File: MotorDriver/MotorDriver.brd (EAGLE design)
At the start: 50 x 50 mm, 58 parts, among them CN1 53375-0610, Q1 BUK7Y7R8-80EX, Q2 BUK7Y7R8-80EX, Q3 BUK7Y7R8-80EX, Q4 BUK7Y7R8-80EX, Q5 BUK7Y7R8-80EX, Q6 BUK7Y7R8-80EX, U1 LPC1549JBD48, U2 DRV8320SRTVT, U3 MCP1700T-33, U4 ADR5041

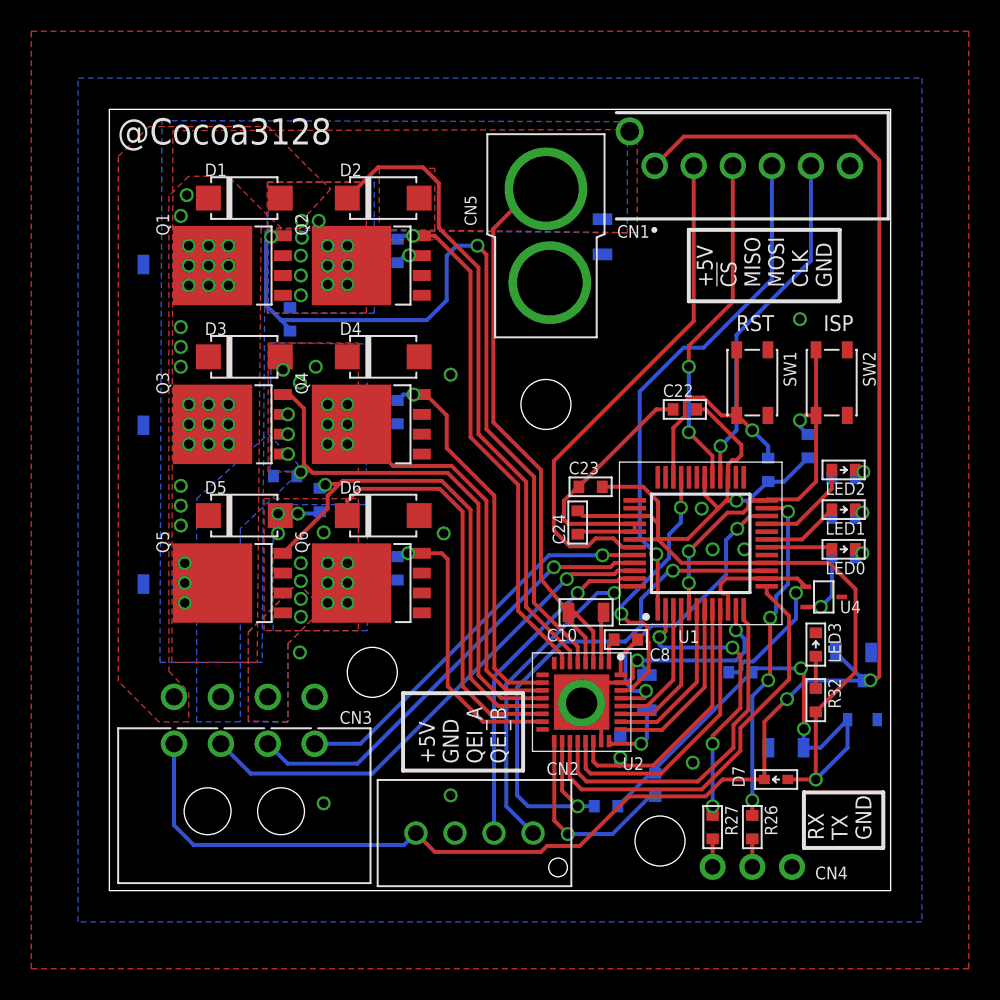
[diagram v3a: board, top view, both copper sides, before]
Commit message: 機能追加 *CANバス *ホールセンサをダイレクトでDRVへ入力 *電源電圧監視 *DCDCをGDに内蔵 *15Aヒューズ
機能削減
*UART-DFUを廃止
*SPI接続を廃止
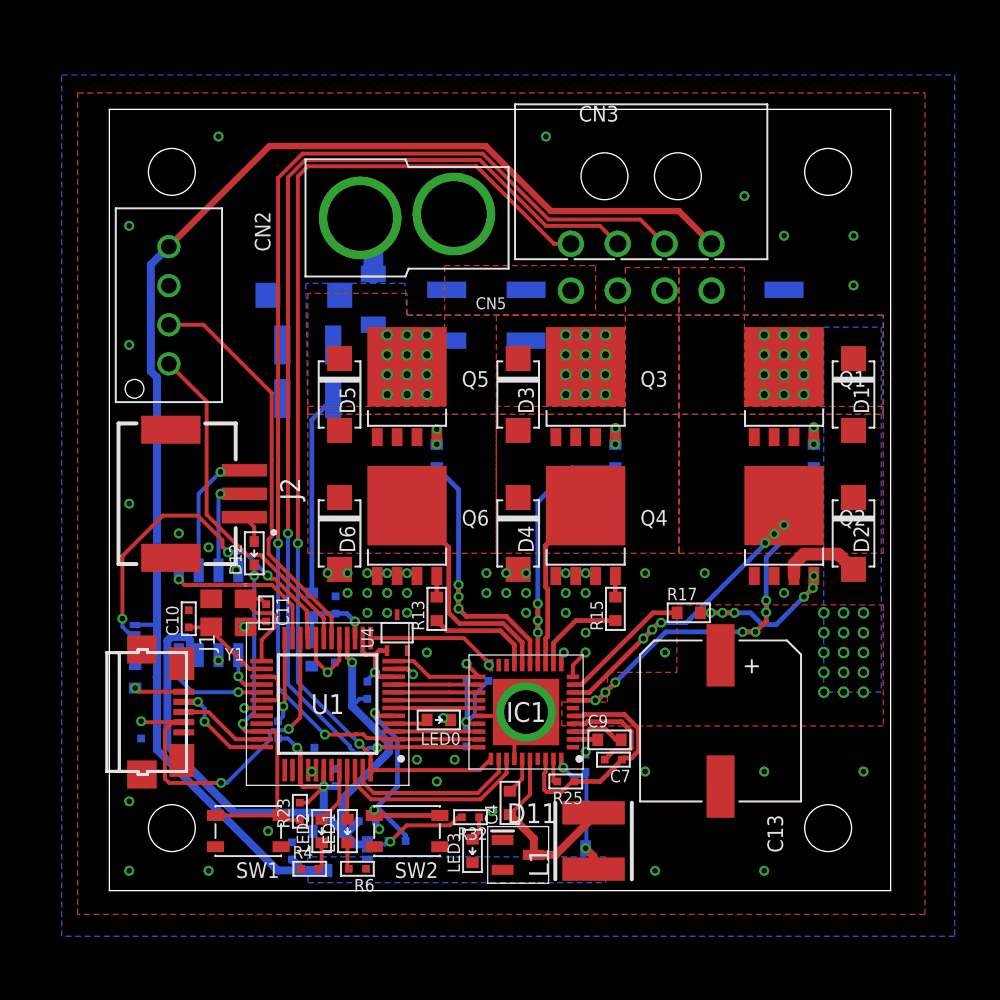
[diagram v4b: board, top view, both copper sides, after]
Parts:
- removed CN1: 53375-0610, MotorDriver:53375-0610
- removed CN4: (no value), nonolith.lbr:1X03_ROUND
- removed R10, R11, R12, R9: 10k, MotorDriver:R1608
- removed R26, R27: 100, MotorDriver:R1608
- removed U2: DRV8320SRTVT, MotorDriver:DRV8320SRTVT
- added C11: 10p, MotorDriver:C1005
- added C12: 10u, MotorDriver:C3225
- added C13: 100u, Passive:ES-10
- added C4: 0.1u, MotorDriver:C1608
- added C5: 0.47u, MotorDriver:C1005
- added C7: 1u, MotorDriver:C1005
- added D10: SMAJ60A, MotorDriver:DO-214AC
- added D11: HSMS-2800-TR1G, HSMS-2800-TR1G:SOT96P240X120-3N
- added D12: (no value), MotorDriver:DIODE_SOD523
- added D8, D9: SDM2U40CSP-7B, SDM2U40CSP-7B:X3-WLB1608-2
- added F1: 15, Passive:3216
- added IC1: DRV8320RSRHAR, DRV8320RSRHAR:QFN50P600X600X100-41N
- added IC2: MAX3051ESA+, MAX3051ESA+:SOIC127P600X175-8N
- added J1: J_USB_MICROAB_HIROSE_ZX62-AB-5PA, j_usb_hirose_zx62-ab-5pa:J_USB_MICROAB_HIROSE_ZX62-AB-5PA
- added J2: SM03B-ZESS-TB, SM03B-ZESS-TB:SM03B-ZESS-TB
- added L1: NR5040T330M, NR5040T330M:NR5040T2R2N
- added R13, R14, R15, R16: 10, MotorDriver:R1608
- added R18: (no value), MotorDriver:R1005
- added R19, R24: 10k, MotorDriver:R1005
- added R20: 47k, MotorDriver:R1608
- added R22: 2.2k, MotorDriver:R1608
- added R25: 100k, MotorDriver:R1005
- added RF1: 900m, Passive:1608
- added Y1: FA238V, FA238V:EPSON_FA238V
- C1, C2, C3, C6: value 1u -> 10u; device MotorDriver:C2012 -> MotorDriver:C3225
- C10: value 1u -> 10p; device MotorDriver:C2012 -> MotorDriver:C1005
- C19, C20: value 1u -> 0.1u; device MotorDriver:C2012 -> MotorDriver:C1005
- C22, C23, C24: device MotorDriver:C1608 -> MotorDriver:C1005
- C8: value 47n -> 1u; device MotorDriver:C1608 -> MotorDriver:C1005
- C9: value 1u -> 47n; device MotorDriver:C2012 -> MotorDriver:C1608
- D1, D2, D3, D4, D5, D6: value (none) -> NRVTSA4100ET3G
- D7: value (none) -> SDM2U40CSP-7B; device MotorDriver:DIODE_SOD523 -> SDM2U40CSP-7B:X3-WLB1608-2
- R1: value 10k -> 12k; device MotorDriver:R1608 -> MotorDriver:R1005
- R17, R3: value 10k -> 10
- R2: value 10k -> 2.2k; device MotorDriver:R1608 -> MotorDriver:R1005
- R21, R23, R32, R4, R5, R6, R7, R8: device MotorDriver:R1608 -> MotorDriver:R1005
- SW1, SW2: device Switch:SKRP -> MotorDriver:SKRP
- U3: device ic-Microchip:SOT23-3 -> MotorDriver:SOT23-3
- U4: device ic-AD:SC70-3 -> MotorDriver:SC70-3
- moved CN3 47.9 mm to (34.0, 45.7), turned to 0 degrees
- moved SW1 43.2 mm to (8.89, 3.81), turned to 180 degrees
- moved R4 42.3 mm to (12.8, 1.40), flipped to the top, turned to 0 degrees
- moved D1 41.0 mm to (47.6, 31.8), turned to 270 degrees
- moved LED2 40.6 mm to (13.6, 3.81), turned to 90 degrees
- moved C1 40.0 mm to (43.2, 36.8), turned to 90 degrees
- moved SW2 39.5 mm to (19.1, 3.81), turned to 180 degrees
- moved CN2 39.0 mm to (3.81, 37.5), turned to 270 degrees
- moved R6 38.4 mm to (15.9, 1.40), flipped to the top
- moved C20 38.1 mm to (11.7, 2.54), turned to 90 degrees
- moved LED1 37.8 mm to (15.2, 3.81), turned to 90 degrees
- moved R23 37.1 mm to (12.2, 5.08), flipped to the top, turned to 90 degrees
- moved D2 37.0 mm to (47.6, 22.9), turned to 270 degrees
- moved Q1 35.8 mm to (43.2, 31.8), turned to 0 degrees
- moved U3 35.6 mm to (14.0, 2.54), turned to 180 degrees
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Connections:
- removed net !CS_DEV: CN1.2, U1.43
- removed net MISO: CN1.3, U1.29
- removed net MOSI: CN1.4, U1.1
- removed net PWM_AL: U1.6, U2.26
- removed net PWM_BH: U1.4, U2.27
- removed net PWM_BL: U1.3, U2.28
- removed net PWM_CH: U1.22, U2.29
- removed net PWM_CL: U1.33, U2.30
- removed net RX: R27.1, U1.2
- removed net SCLK_DEV: CN1.5, U1.28
- removed net TX: R26.1, U1.23
- new net !BRAKE: IC1.33, U1.46
- new net CANH: IC2.7, J2.2
- new net CANL: IC2.6, J2.3
- new net CAN_RX: IC2.4, U1.29
- new net CAN_TX: IC2.1, U1.28
- new net D+: J1.P$3, U1.35
- new net D-: J1.P$2, U1.36
- new net DIR: IC1.32, U1.47
- new net ID: J1.P$4, R8.2, U1.22
- new net N$11: Q3.4, R14.2
- new net N$12: Q6.4, R13.2
- new net N$13: Q5.4, R3.2
- new net N$14: J1.P$1, RF1.1
- new net N$15: R18.2, U1.24
- new net N$16: C7.2, IC1.4
- new net N$17: C8.1, IC1.27, R19.2, R24.2
- new net N$18: C9.1, IC1.2
- new net N$19: C9.2, IC1.3
- new net N$20: IC1.39, R25.2
- new net N$21: C11.1, U1.25, Y1.1
- new net N$22: C10.1, U1.26, Y1.3
- new net N$23: U1.27, U1.30
- new net N$24: D12.A, J2.1
- new net N$26: CN5.P, F1.2
- new net N$4: C4.2, IC1.35
- new net SHDN: IC2.5, U1.23
- new net VBAT: C5.2, R20.1, R22.2, U1.15
- new net VBUS: D9.2, RF1.2, U1.21
- net !CS: now also IC1.24, U1.7; no longer U1.9, U2.21
- net !FAULT: now also IC1.20, R24.1, U1.13; no longer R1.1, U2.17
- net !ISP: now also R7.1; no longer R17.1, U1.24
- net !RST: now also D12.K
- net +3V3: now also D7.2, IC2.3, R18.1, R7.2; no longer D7.A, R1.2, R17.2, R2.2, U1.27, U1.30
- net +5V: now also D7.1, D8.1, D9.1; no longer CN1.1, D7.K
- net GH_A: now also IC1.7, R16.1; no longer Q1.4, R11.2, U2.5
- net GH_B: now also IC1.14, R14.1; no longer Q3.4, R9.2, U2.12
- net GH_C: now also IC1.15, R3.1; no longer Q5.4, R7.2, U2.13
- net GL_A: now also IC1.9, R17.1; no longer Q2.4, R12.2, U2.7
- net GL_B: now also IC1.12, R15.1; no longer Q4.4, R10.2, U2.10
- net GL_C: now also IC1.17, R13.1; no longer Q6.4, R8.2, U2.15
- net GND: now also C10.2, C11.2, C12.2, C13.N, C5.1, C8.2, CN3.6, D10.A, D11.1, IC1.1, IC1.10, IC1.11, IC1.18, IC1.19, IC1.26, IC1.34, IC1.41, IC2.2, IC2.8, J1.P$5, J1.SHIELD1, J1.SHIELD2, J1.SHIELD3, J1.SHIELD4, R2.2, R22.1, Y1.2, Y1.4; no longer C9.2, CN1.6, CN3.5, CN4.1, R10.1, R12.1, R3.1, U2.16, U2.23, U2.31, U2.33, U2.8, U2.9
- net HALL_U: now also IC1.29, U1.2; no longer U1.46
- net HALL_V: now also IC1.30, U1.1; no longer U1.45
- net HALL_W: now also IC1.31, U1.48; no longer U1.44
- net LED0: now also U1.4; no longer U1.18
- net LED1: now also U1.45; no longer U1.19
- net LED2: now also U1.44; no longer U1.21
- net N$1: now also IC1.40, R1.2, R2.1; no longer CN4.2, R26.2
- net N$2: now also D8.2, L1.1, R1.1; no longer CN4.3, R27.2
- net N$3: now also C4.1, D11.3, IC1.36, L1.2; no longer C10.1, U2.2
- net N$5: now also Q2.4, R17.2; no longer C8.1, U2.1
- net N$6: now also Q1.4, R16.2; no longer C8.2, U2.32
- net N$7: now also Q4.4, R15.2; no longer C9.1, U2.24
- net PWM_AH: now also IC1.28, U1.3; no longer U1.7, U2.25
- net PWM_EN: now also IC1.25, U1.6; no longer R3.2, U1.8, U2.22
- net QEI_A: now also U1.18; no longer U1.47
- net QEI_B: now also U1.19; no longer U1.48
- net SCLK: now also IC1.23, U1.8; no longer U1.12, U2.20
- net SDI: now also IC1.22, U1.9; no longer U1.13, U2.19
- net SDO: now also IC1.21, R19.1, U1.12; no longer R2.1, U1.15, U2.18
- net SH_A: now also IC1.8; no longer R11.1, U2.6
- net SH_B: now also IC1.13; no longer R9.1, U2.11
- net SH_C: now also CN3.5, IC1.16; no longer CN3.6, R7.1, U2.14
- net V+: now also C12.1, C13.P, C7.1, D10.K, F1.1, IC1.38, IC1.5, IC1.6, R20.2, R25.1; no longer C10.2, CN5.P, U2.3, U2.4
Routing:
- net HALL_W: track 25.5 -> 67.7 mm, vias 1 -> 2
- net HALL_U: track 32.7 -> 74.7 mm, vias 1 -> 2
- net HALL_V: track 29.3 -> 70.5 mm, vias 1 -> 2
- net +3V3: track 93.6 -> 60.0 mm
- net MOSI: track 33.1 -> 0.00 mm, vias 1 -> 0
- net !CS_DEV: track 33.1 -> 0.00 mm
- net SDO: track 36.8 -> 7.07 mm, vias 2 -> 1
- net VBUS: track 0.00 -> 24.7 mm, vias 0 -> 3
- net GL_A: track 33.2 -> 8.57 mm, vias 1 -> 0
- net GH_A: track 53.2 -> 28.9 mm, vias 2 -> 7
- net ID: track 0.00 -> 23.1 mm, vias 0 -> 3
- net SCLK_DEV: track 22.3 -> 0.00 mm, vias 1 -> 0
- net GND: track 45.6 -> 23.4 mm, vias 15 -> 66
- net TX: track 21.9 -> 0.00 mm, vias 4 -> 0
- net MISO: track 21.7 -> 0.00 mm, vias 2 -> 0
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- added copper zone on layer 16, net +5V
- removed copper zone on layer 16, net SH_A
- removed copper zone on layer 16, net SH_B
- removed copper zone on layer 16, net SH_C
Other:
- board text removed: "+5V !CS MISO MOSI CLK GND"
- board text removed: "+5V GND QEI_A QEI_B"
- board text removed: "@Cocoa3128"
- board text removed: "ISP"
- board text removed: "RST"
- board text removed: "RX TX GND"

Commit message: ヒューズ切断検出機能を追加
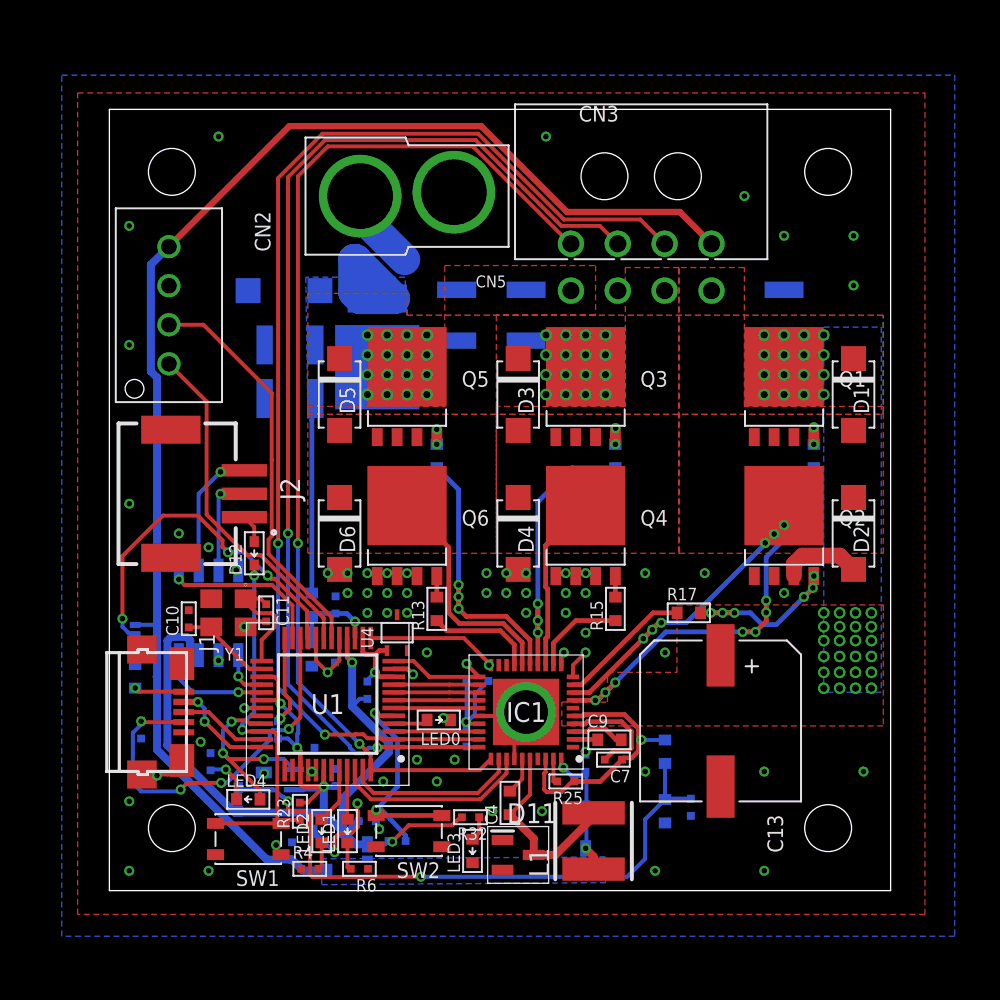
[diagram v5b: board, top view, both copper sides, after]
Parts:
- added C14: 0.47u, MotorDriver:C1005
- added D13: TSPB20U80S S1G, Diode:SMPC
- added D14: RB520S, MotorDriver:DIODE_SOD523
- added LED4: (no value), MotorDriver:LED1608
- added R10: 2.2k, MotorDriver:R1608
- added R11: 330, MotorDriver:R1005
- added R9: 33k, MotorDriver:R1608
- added U2: ADCMP350YKSZ, adcmp350:KS_4
- moved F1 2.57 mm to (17.3, 40.4), turned to 180 degrees
- moved CN5 1.40 mm to (19.1, 44.5)
- moved D10 1.30 mm to (11.2, 38.4)
- moved C12 1.14 mm to (11.6, 34.9)
- moved C6 1.14 mm to (11.6, 31.5)
- moved C3 0.64 mm to (22.2, 36.8)
- moved SW1 0.51 mm to (8.89, 3.30)
- moved R6 0.13 mm to (16.0, 1.40)
- moved SW2 0.13 mm to (19.2, 3.81)
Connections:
- new net FUSE: LED4.A, U1.33, U2.3
- new net N$25: C14.2, D14.A, R10.2, R9.1, U2.1
- new net N$27: LED4.K, R11.2
- net +3V3: now also D14.K, U1.27, U1.30, U2.4
- net GND: now also C14.1, R10.1, R11.1, U2.2
- net N$23: now also D13.1, D13.2, F1.1; no longer U1.27, U1.30
- net V+: now also D13.K, R9.2; no longer F1.1
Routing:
- net N$25: track 0.00 -> 41.4 mm, vias 0 -> 2
- net FUSE: track 0.00 -> 13.2 mm, vias 0 -> 3
- net +3V3: track 60.0 -> 69.4 mm, vias 4 -> 5
- net GND: track 23.4 -> 32.4 mm, vias 66 -> 73
- net N$23: track 3.39 -> 8.48 mm
- net N$27: track 0.00 -> 3.19 mm, vias 0 -> 1
- net ID: track 23.1 -> 25.9 mm, vias 3 -> 4
- net +5V: track 91.1 -> 89.6 mm
- net N$26: track 3.93 -> 5.24 mm
- net V+: track 28.3 -> 29.4 mm, vias 51 -> 73
- net HALL_V: track 70.5 -> 71.6 mm
- net HALL_W: track 67.7 -> 68.8 mm
- net HALL_U: track 74.7 -> 75.7 mm
- net !RST: track 23.9 -> 24.5 mm

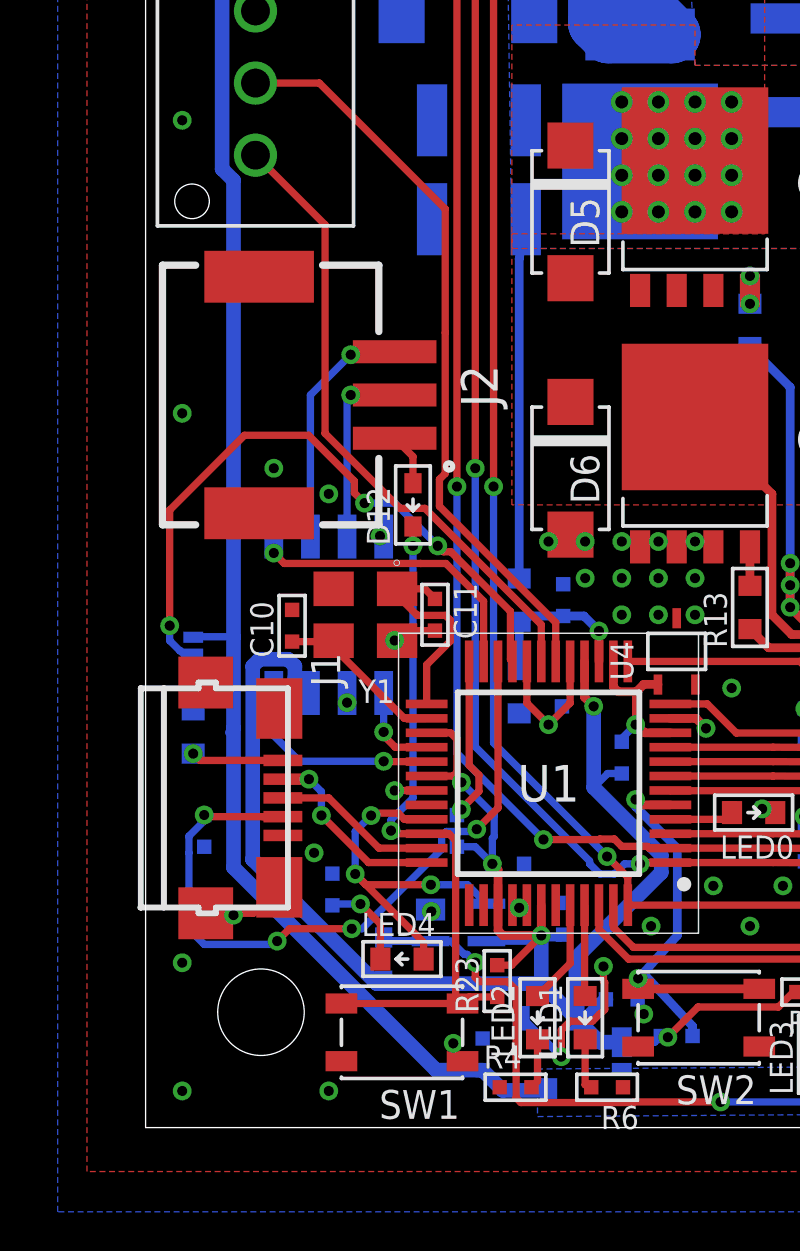
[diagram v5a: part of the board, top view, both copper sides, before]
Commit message: USBラインの保護を強化した
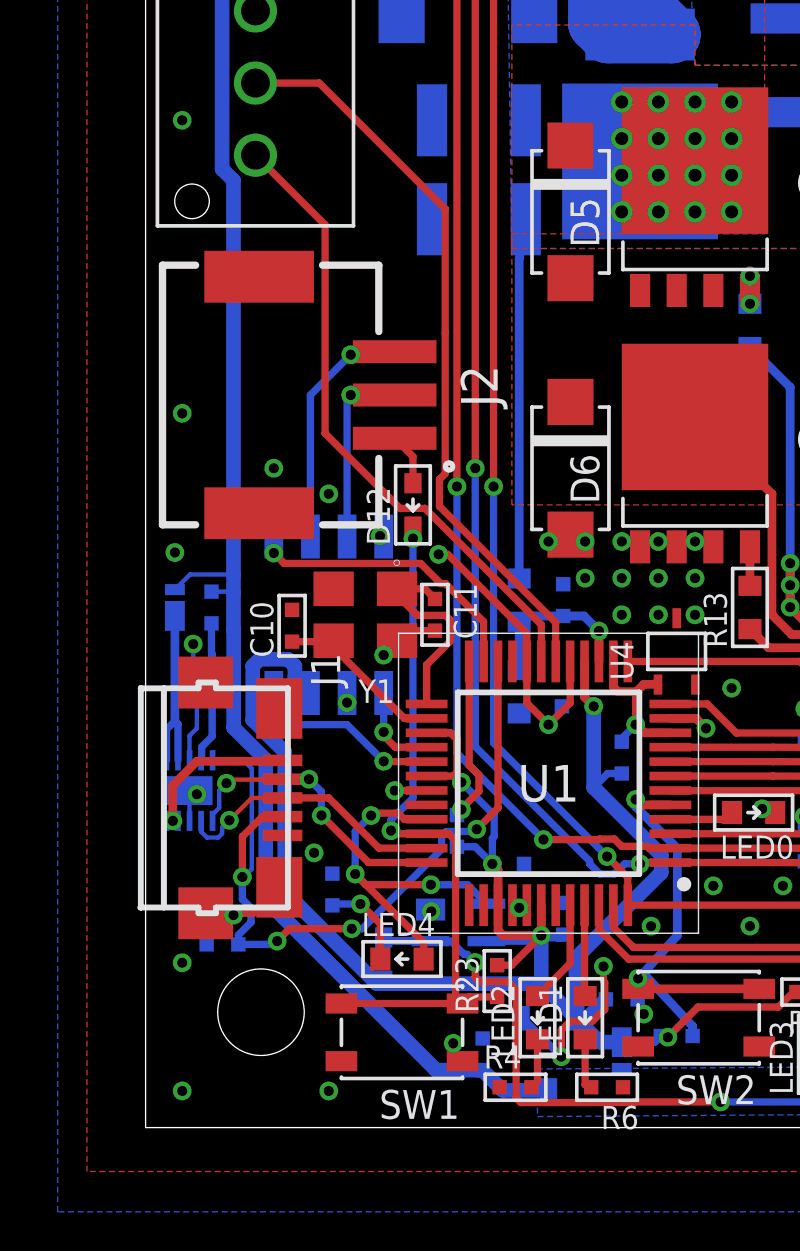
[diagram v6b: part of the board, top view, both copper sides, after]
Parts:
- removed RF1: 900m, Passive:1608
- added IC3: TPD4S014DSQR, TPD4S014DSQR:SON40P200X200X80-11N
- added R12, R26: 2.2k, MotorDriver:R1005
- moved R8 3.99 mm to (2.67, 6.35), turned to 180 degrees
- moved D9 1.77 mm to (1.02, 18.0)
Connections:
- new net N$28: IC3.3, R26.2
- new net N$29: IC3.4, R12.1
- net +5V: now also R12.2
- net D+: now also IC3.7
- net D-: now also IC3.6
- net GND: now also IC3.11, IC3.8, R26.1
- net ID: now also IC3.5
- net N$14: now also IC3.10, IC3.9; no longer RF1.1
- net VBUS: now also IC3.1, IC3.2; no longer RF1.2, U1.21
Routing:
- net VBUS: track 24.7 -> 6.54 mm, vias 3 -> 0
- net GND: track 32.4 -> 39.4 mm, vias 73 -> 77
- net N$29: track 0.00 -> 4.92 mm
- net D+: track 5.71 -> 9.89 mm, vias 0 -> 1
- net D-: track 6.67 -> 10.2 mm, vias 2 -> 3
- net N$14: track 3.21 -> 5.81 mm
- net N$28: track 0.00 -> 2.32 mm
- net ID: track 25.9 -> 27.5 mm
- net +5V: track 89.6 -> 91.0 mm
